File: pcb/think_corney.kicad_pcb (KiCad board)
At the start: 2 copper layers, 128.5 x 87.4 mm, 56 parts

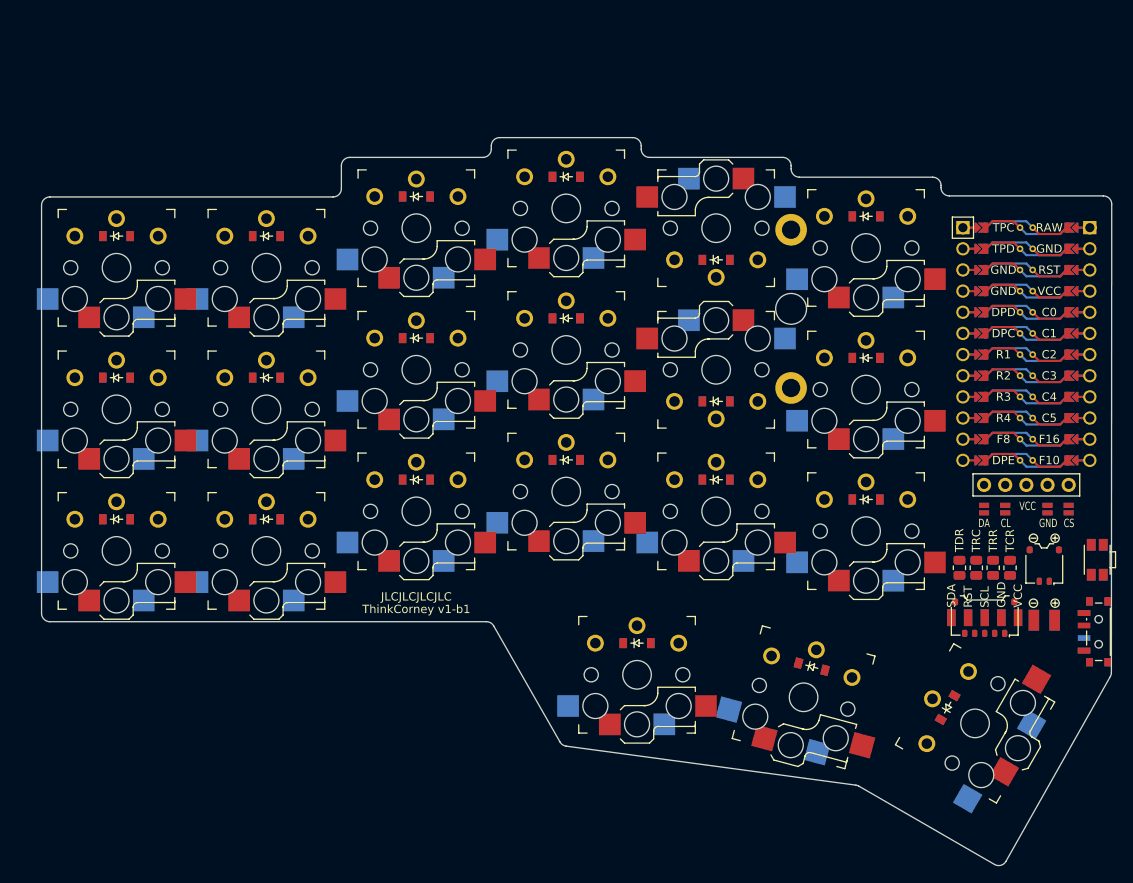
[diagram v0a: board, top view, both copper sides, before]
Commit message: KiCad: Fix many DRC problems
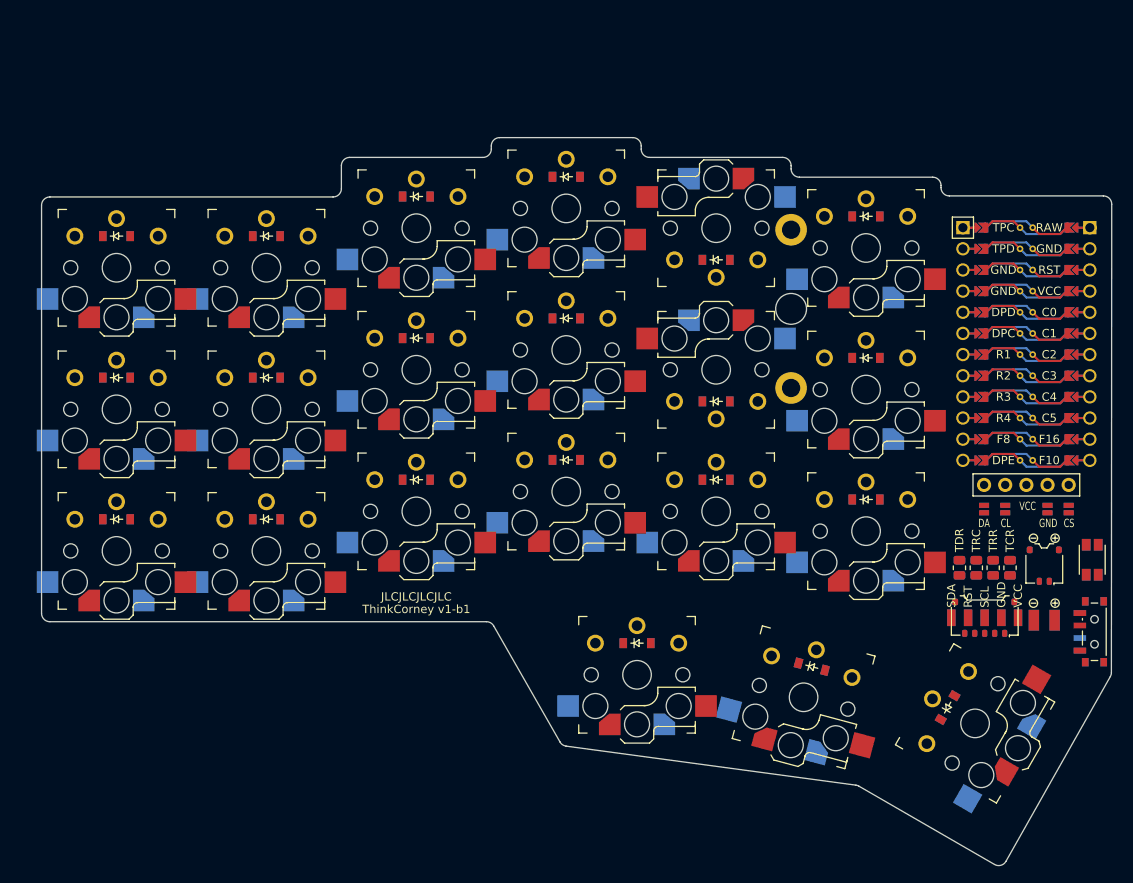
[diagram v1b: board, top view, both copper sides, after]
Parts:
- removed CONN3: , sw_reset_side
- added SW2: , sw_reset_side, F.Cu at (217.2, 101.1)
- moved SW1 0.50 mm to (217.4, 109.7)

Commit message: KiCad: Updated PCB to latest ergogen generated version
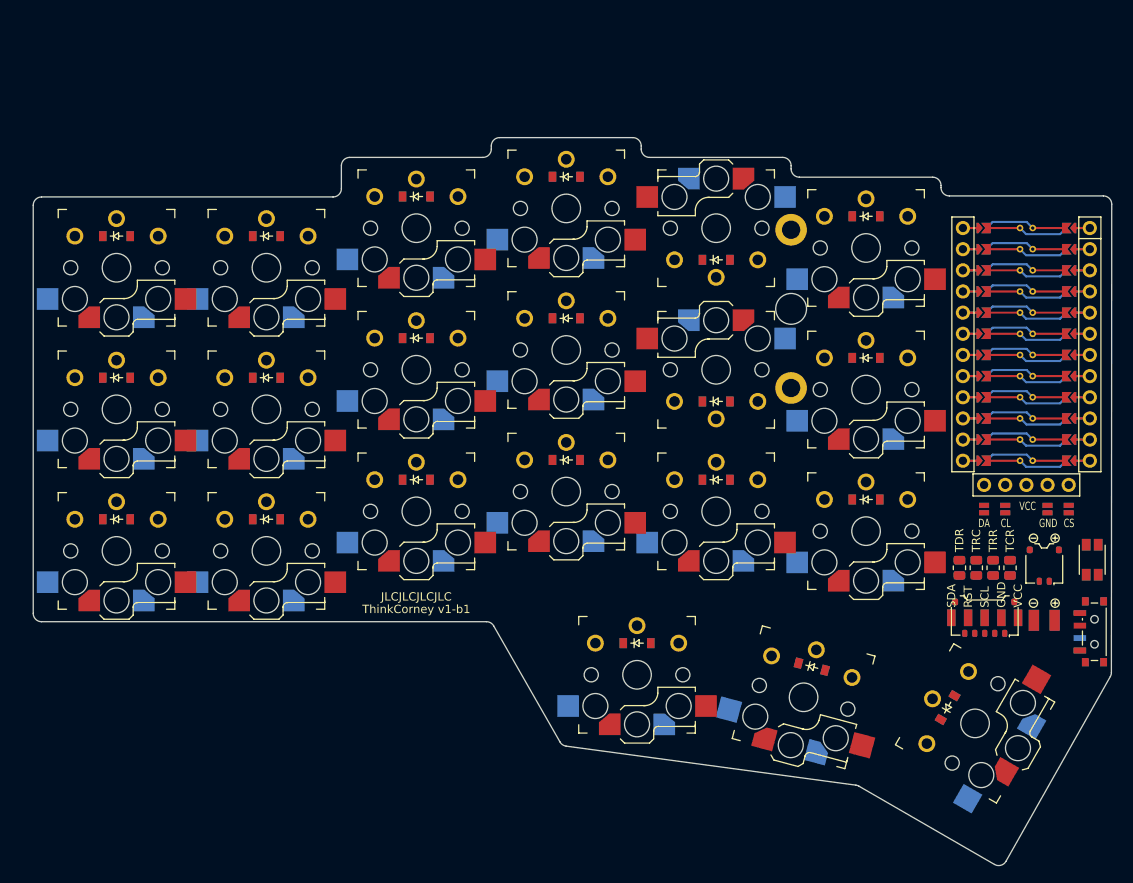
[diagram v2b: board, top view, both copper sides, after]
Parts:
- removed ? (x2): , text
- removed _1: , ProMicro
- added MCU1: , nice_nano, F.Cu at (209.2, 73.9)
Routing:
- net GND: track 0.00 -> 30.5 mm
- net TPC: track 0.00 -> 10.2 mm
- net R3: track 0.00 -> 10.2 mm
- net F8: track 0.00 -> 10.2 mm
- net DPE: track 0.00 -> 10.2 mm
- net DPD: track 0.00 -> 10.2 mm
- net C5: track 0.00 -> 10.2 mm
- net C4: track 0.00 -> 10.2 mm
- net C3: track 0.00 -> 10.2 mm
- net C2: track 0.00 -> 10.2 mm
- net C0: track 0.00 -> 10.2 mm
- net RST: track 0.00 -> 10.2 mm
- net R1: track 0.00 -> 10.2 mm
- net F10: track 0.00 -> 10.2 mm
- net C1: track 0.00 -> 10.2 mm
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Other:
- board size 128.5 x 87.4 mm -> 129.5 x 87.4 mm
- board text added: "JLCJLCJLCJLC"
- board text added: "ThinkCorney v1-b1"

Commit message: PCB: Update to latest pcb version with initial traces
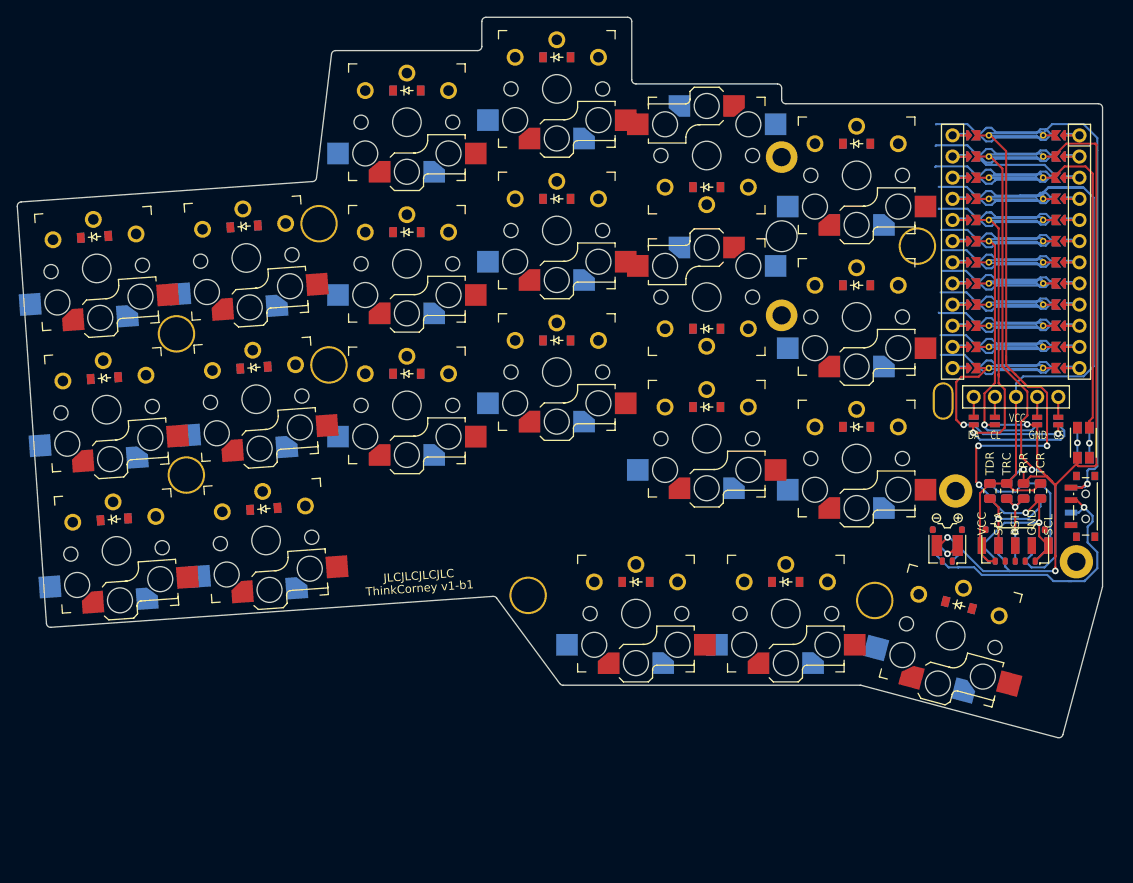
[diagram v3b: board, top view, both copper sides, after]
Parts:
- removed ICON2: , icon_bat
- added H1: , mounting_hole, F.Cu at (199.3, 82.0)
- added H10: , mounting_hole, F.Cu at (215.3, 101.3)
- added H2: , mounting_hole, F.Cu at (107.2, 73.9)
- added H3: , mounting_hole, F.Cu at (108.4, 90.9)
- added H4: , mounting_hole, F.Cu at (124.3, 60.7)
- added H5: , mounting_hole, F.Cu at (125.5, 77.7)
- added H6: , mounting_hole, F.Cu at (196.2, 63.4)
- added H7: , mounting_hole, F.Cu at (149.4, 105.3)
- added H8: , mounting_hole, F.Cu at (191.0, 106.0)
- added H9: , mounting_hole, F.Cu at (200.8, 92.8)
- added P1": , point_debugger, F.Cu at (100.0, 100.0)
- added P10": , point_debugger, F.Cu at (152.9, 78.5)
- added P11": , point_debugger, F.Cu at (152.9, 61.5)
- added P12": , point_debugger, F.Cu at (152.9, 44.5)
- added P13": , point_debugger, F.Cu at (170.9, 86.5)
- added P14": , point_debugger, F.Cu at (170.9, 69.5)
- added P15": , point_debugger, F.Cu at (170.9, 52.5)
- added P16": , point_debugger, F.Cu at (188.9, 88.9)
- added P17": , point_debugger, F.Cu at (188.9, 71.9)
- added P18": , point_debugger, F.Cu at (188.9, 54.9)
- added P19": , point_debugger, F.Cu at (162.4, 107.5)
- added P2": , point_debugger, F.Cu at (98.8, 83.0)
- added P20": , point_debugger, F.Cu at (180.4, 107.5)
- added P21": , point_debugger, F.Cu at (200.2, 110.2)
- added P22": , point_debugger, F.Cu at (208.0, 62.8)
- added P23": , point_debugger, F.Cu at (200.8, 92.8)
- added P24": , point_debugger, F.Cu at (215.3, 101.3)
- added P25": , point_debugger, F.Cu at (218.4, 46.3)
- added P26": , point_debugger, F.Cu at (218.4, 99.3)
- added P27", P28": , point_debugger, F.Cu at (218.4, 104.3)
- added P29": , point_debugger, F.Cu at (198.0, 118.4)
- added P3": , point_debugger, F.Cu at (97.6, 66.1)
- added P30": , point_debugger, F.Cu at (213.5, 122.5)
- added P31": , point_debugger, F.Cu at (145.5, 105.3)
- added P32": , point_debugger, F.Cu at (153.4, 105.3)
- added P33": , point_debugger, F.Cu at (208.0, 64.8)
- added P34": , point_debugger, F.Cu at (199.3, 82.0)
- added P35", P36": , point_debugger, F.Cu at (199.8, 99.4)
- added P37": , point_debugger, F.Cu at (216.3, 94.7)
- added P38": , point_debugger, F.Cu at (216.1, 87.0)
- added P39": , point_debugger, F.Cu at (179.9, 62.2)
- added P4": , point_debugger, F.Cu at (118.0, 98.7)
- added P40": , point_debugger, F.Cu at (207.9, 99.4)
- added P41": , point_debugger, F.Cu at (207.9, 92.8)
- added P42": , point_debugger, F.Cu at (136.4, 104.5)
- added P43": , point_debugger, F.Cu at (107.2, 73.9)
- added P44": , point_debugger, F.Cu at (108.4, 90.9)
- added P45": , point_debugger, F.Cu at (124.3, 60.7)
- added P46": , point_debugger, F.Cu at (125.5, 77.7)
- added P47": , point_debugger, F.Cu at (196.2, 63.4)
- added P48": , point_debugger, F.Cu at (149.4, 105.3)
- added P49": , point_debugger, F.Cu at (191.0, 106.0)
- added P5": , point_debugger, F.Cu at (116.8, 81.8)
- added P6": , point_debugger, F.Cu at (115.6, 64.8)
- added P7": , point_debugger, F.Cu at (134.9, 82.5)
- added P8": , point_debugger, F.Cu at (134.9, 65.5)
- added P9": , point_debugger, F.Cu at (134.9, 48.5)
- moved SW1 15.1 mm to (216.3, 94.7)
- moved PAD1 14.7 mm to (199.8, 99.4)
- moved D10 14.4 mm to (152.9, 74.7)
- moved D11 14.4 mm to (152.9, 57.7)
- moved D12 14.4 mm to (152.9, 40.7)
- moved S10 14.4 mm to (152.9, 78.5)
- moved S11 14.4 mm to (152.9, 61.5)
- moved S12 14.4 mm to (152.9, 44.5)
- moved SW2 14.1 mm to (216.1, 87.0)
- moved D7 12.8 mm to (134.9, 78.7)
- moved D8 12.8 mm to (134.9, 61.7)
- moved D9 12.8 mm to (134.9, 44.7)
- moved S7 12.8 mm to (134.9, 82.5)
- moved S8 12.8 mm to (134.9, 65.5)
- moved S9 12.8 mm to (134.9, 48.5)
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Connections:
- CONN2 pad 1: VCC -> TPC
- CONN2 pad 3: TPC -> TPR
- CONN2 pad 4: TPR -> TPD
- CONN2 pad 5: TPD -> VCC
- PAD2 pad 1: TPD -> VCC
- PAD2 pad 2: TPR -> TPD
- PAD2 pad 3: TPC -> TPR
- PAD2 pad 5: VCC -> TPC
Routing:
- net GND: track 30.5 -> 182.0 mm, vias 0 -> 5
- net VCC: track 10.2 -> 118.1 mm
- net F16: track 10.2 -> 84.6 mm, vias 0 -> 5
- net RAW: track 10.2 -> 78.7 mm, vias 0 -> 1
- net TPD: track 10.2 -> 74.1 mm, vias 0 -> 2
- net TPC: track 10.2 -> 68.0 mm, vias 0 -> 1
- net RST: track 10.2 -> 63.4 mm, vias 0 -> 1
- net F10: track 10.2 -> 58.9 mm, vias 0 -> 1
- net BAT_P: track 0.00 -> 38.4 mm, vias 0 -> 2
- net (no net): track 0.00 -> 36.3 mm
- net DPD: track 10.2 -> 31.4 mm
- net R3: track 10.2 -> 30.2 mm, vias 0 -> 2
- net DPC: track 10.2 -> 25.4 mm
- net C0: track 10.2 -> 24.0 mm
- net C5: track 10.2 -> 23.5 mm
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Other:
- board size 129.5 x 87.4 mm -> 130.3 x 86.5 mm

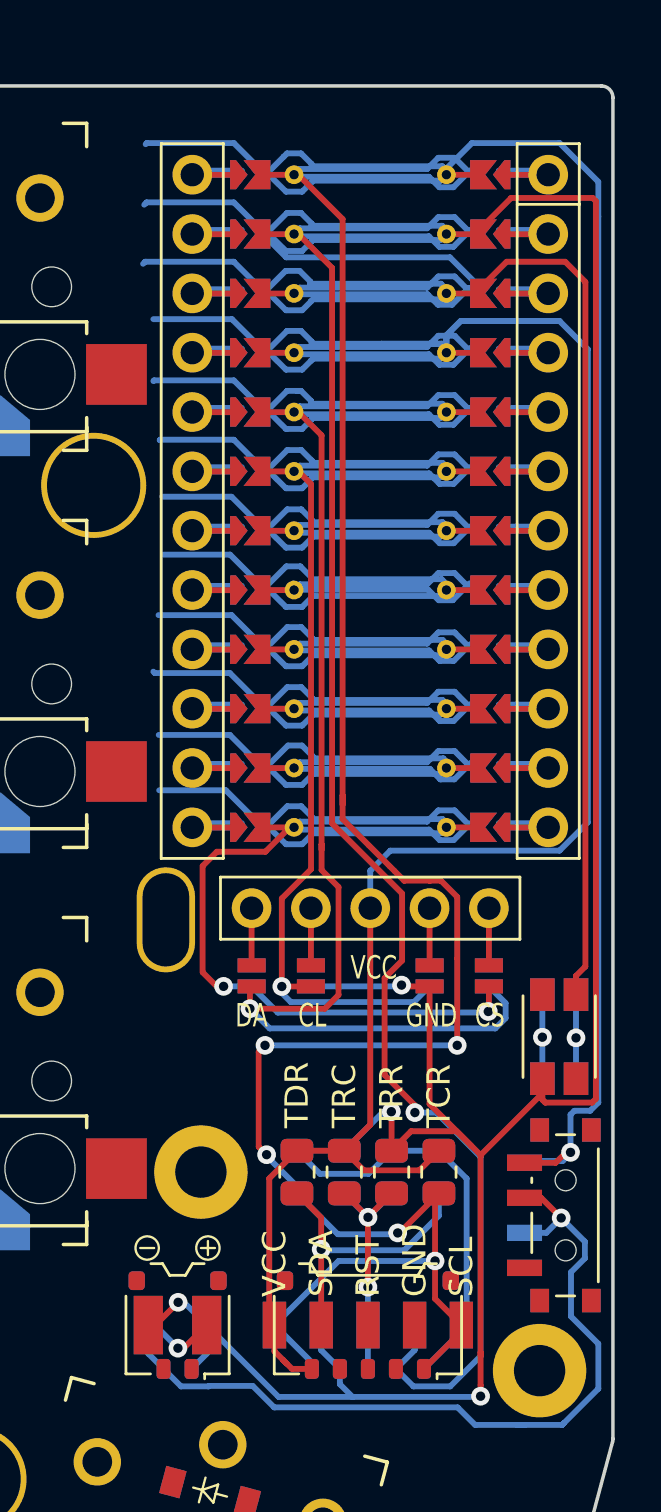
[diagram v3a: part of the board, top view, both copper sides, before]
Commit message: Git: Ignore svg files in pcb dir
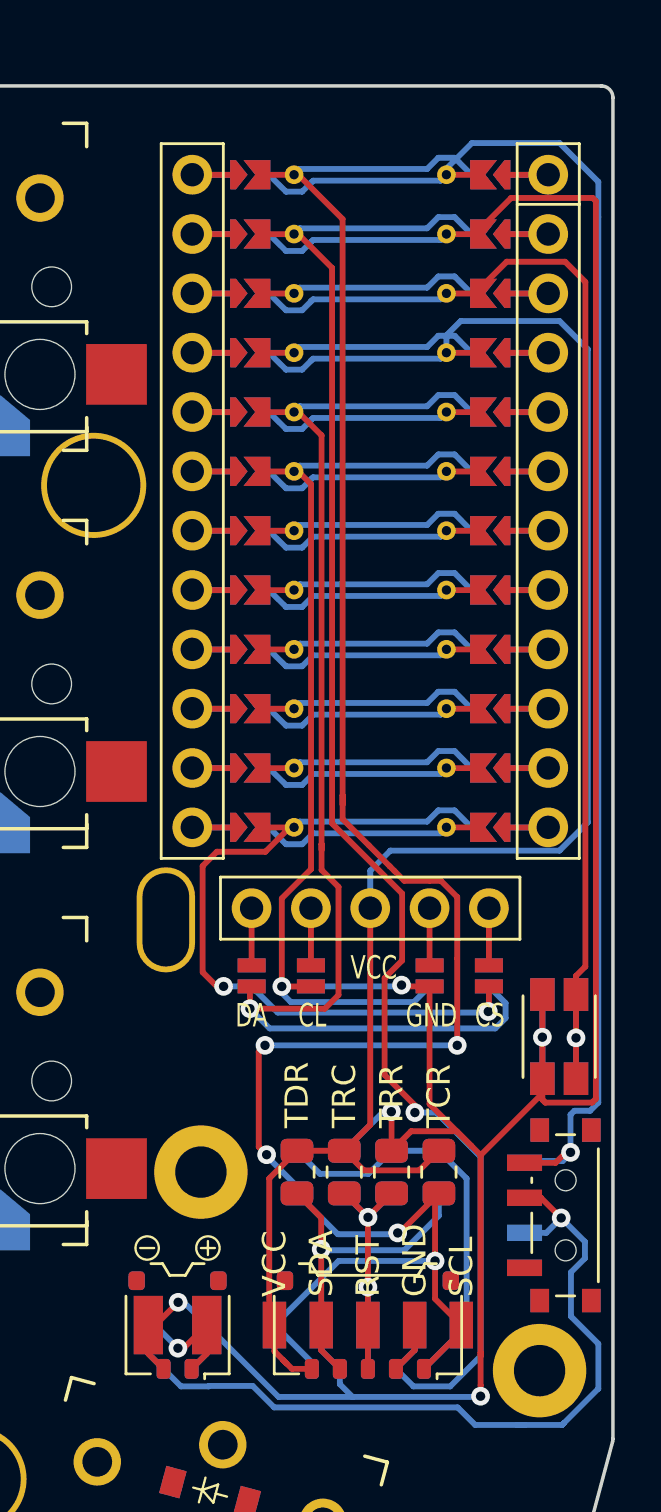
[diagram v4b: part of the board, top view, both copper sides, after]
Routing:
- net TPC: track 68.0 -> 10.2 mm, vias 1 -> 0
- net F10: track 58.9 -> 10.1 mm, vias 1 -> 0
- net (no net): track 36.3 -> 0.00 mm
- net GND: track 182.0 -> 149.3 mm
- net DPD: track 31.4 -> 54.5 mm, vias 0 -> 1
- net VCC: track 118.1 -> 96.3 mm
- net R3: track 30.2 -> 10.2 mm, vias 2 -> 0
- net DPC: track 25.4 -> 41.5 mm, vias 0 -> 1
- net C0: track 24.0 -> 10.1 mm
- net RAW: track 78.7 -> 65.0 mm
- net C5: track 23.5 -> 10.1 mm
- net C4: track 23.2 -> 10.1 mm
- net C1: track 23.2 -> 10.1 mm
- net C2: track 23.1 -> 10.1 mm
- net C3: track 23.0 -> 10.1 mm
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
